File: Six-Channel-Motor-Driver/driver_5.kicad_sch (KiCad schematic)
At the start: 9 parts, among them J2 Screw_Terminal_01x02, Q1 Q_NMOS_GDS, Q2 Q_NMOS_GDS, Q3 Q_NMOS_GDS, Q4 Q_NMOS_GDS

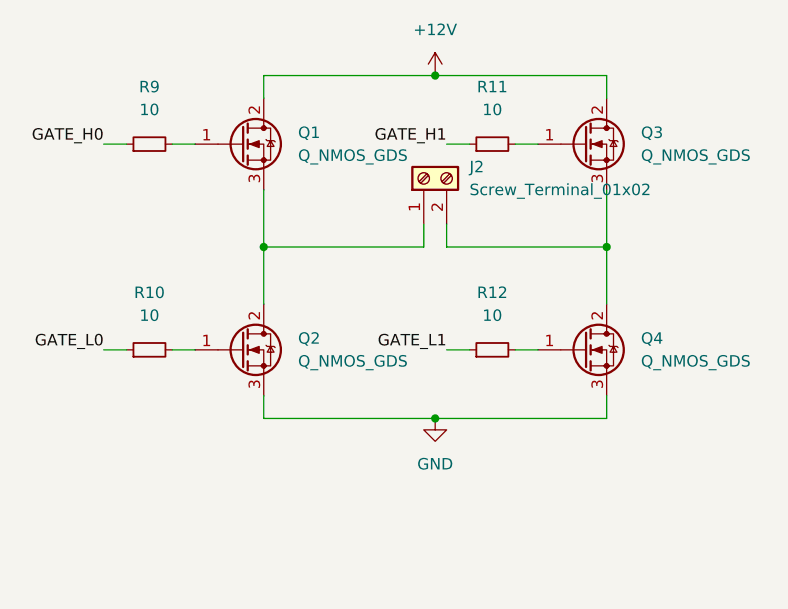
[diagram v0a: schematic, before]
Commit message: Added start of driver blocks
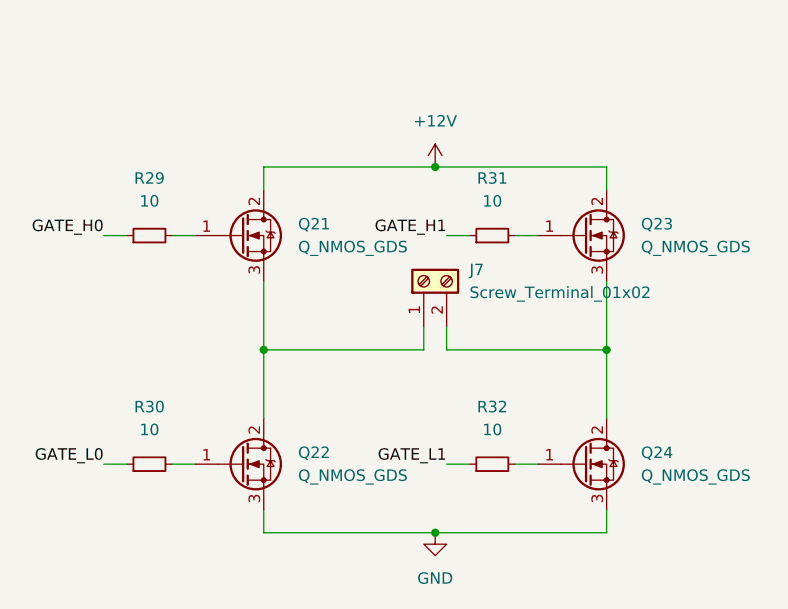
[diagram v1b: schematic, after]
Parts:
- removed J2: Screw_Terminal_01x02, Connector_Wire:SolderWire-2.5sqmm_1x02_P8.8mm_D2.4mm_OD4.4mm, symbol Connector:Screw_Terminal_01x02
- removed Q1, Q2, Q3, Q4: Q_NMOS_GDS, Package_TO_SOT_SMD:SOT-23, symbol Device:Q_NMOS_GDS
- removed R10, R11, R12, R9: 10, Resistor_SMD:R_0603_1608Metric, symbol Device:R_Small
- added J7: Screw_Terminal_01x02, Connector_Wire:SolderWire-2.5sqmm_1x02_P8.8mm_D2.4mm_OD4.4mm, symbol Connector:Screw_Terminal_01x02
- added Q21, Q22, Q23, Q24: Q_NMOS_GDS, Package_TO_SOT_SMD:SOT-23, symbol Device:Q_NMOS_GDS
- added R29, R30, R31, R32: 10, Resistor_SMD:R_0603_1608Metric, symbol Device:R_Small
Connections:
- net +12V: now also Q21.2 (D), Q23.2 (D)
- net GATE_H0: now also R29.1
- net GATE_H1: now also R31.1
- net GATE_L0: now also R30.1
- net GATE_L1: now also R32.1
- net GND: now also Q22.3 (S), Q24.3 (S)
- new net: Q24.1 (G), R32.2
- new net: Q23.1 (G), R31.2
- new net: J7.2 (Pin_2), Q23.3 (S), Q24.2 (D)
- new net: J7.1 (Pin_1), Q21.3 (S), Q22.2 (D)
- new net: Q22.1 (G), R30.2
- new net: Q21.1 (G), R29.2
